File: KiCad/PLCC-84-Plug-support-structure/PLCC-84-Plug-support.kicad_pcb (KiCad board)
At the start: 2 copper layers, 29.6 x 29.6 mm, 4 parts, among them J1 Conn_01x01, J2 Conn_01x01, J3 Conn_01x01, J4 Conn_01x01

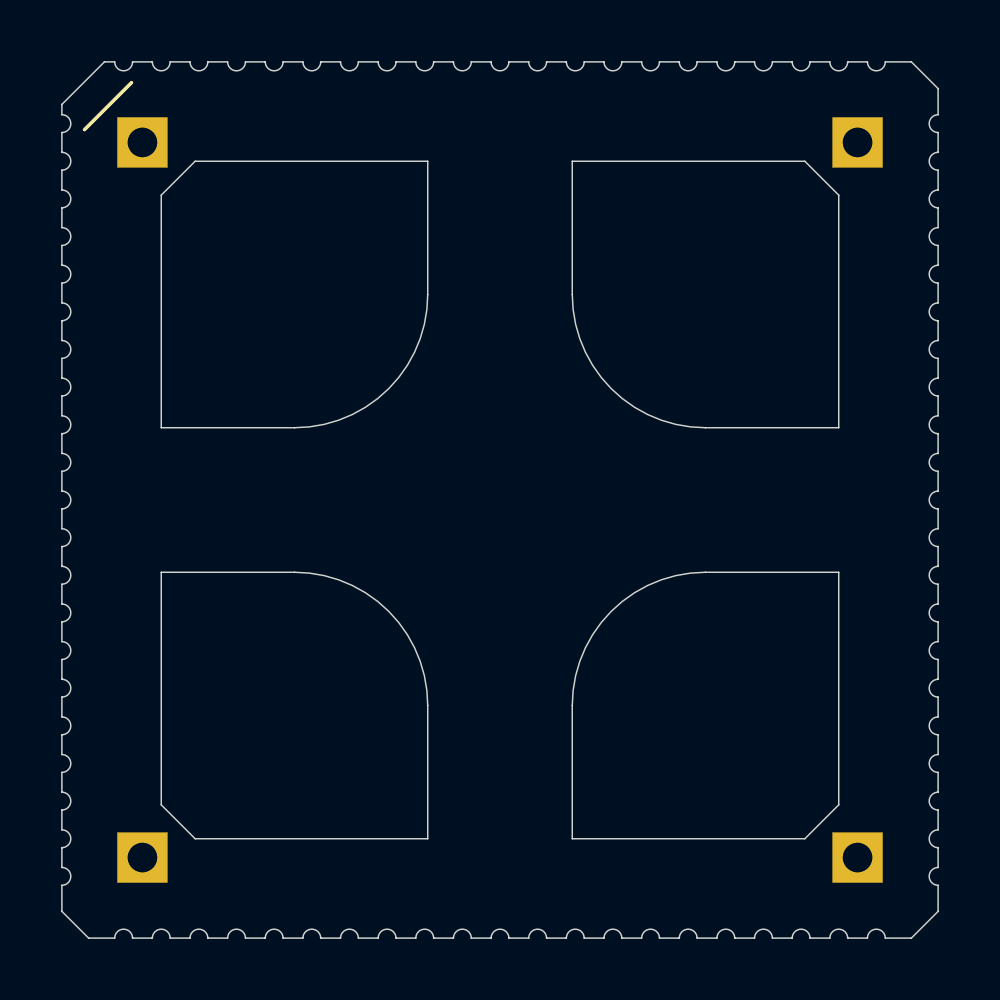
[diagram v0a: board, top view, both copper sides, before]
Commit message: made a new revision 1B with modified size
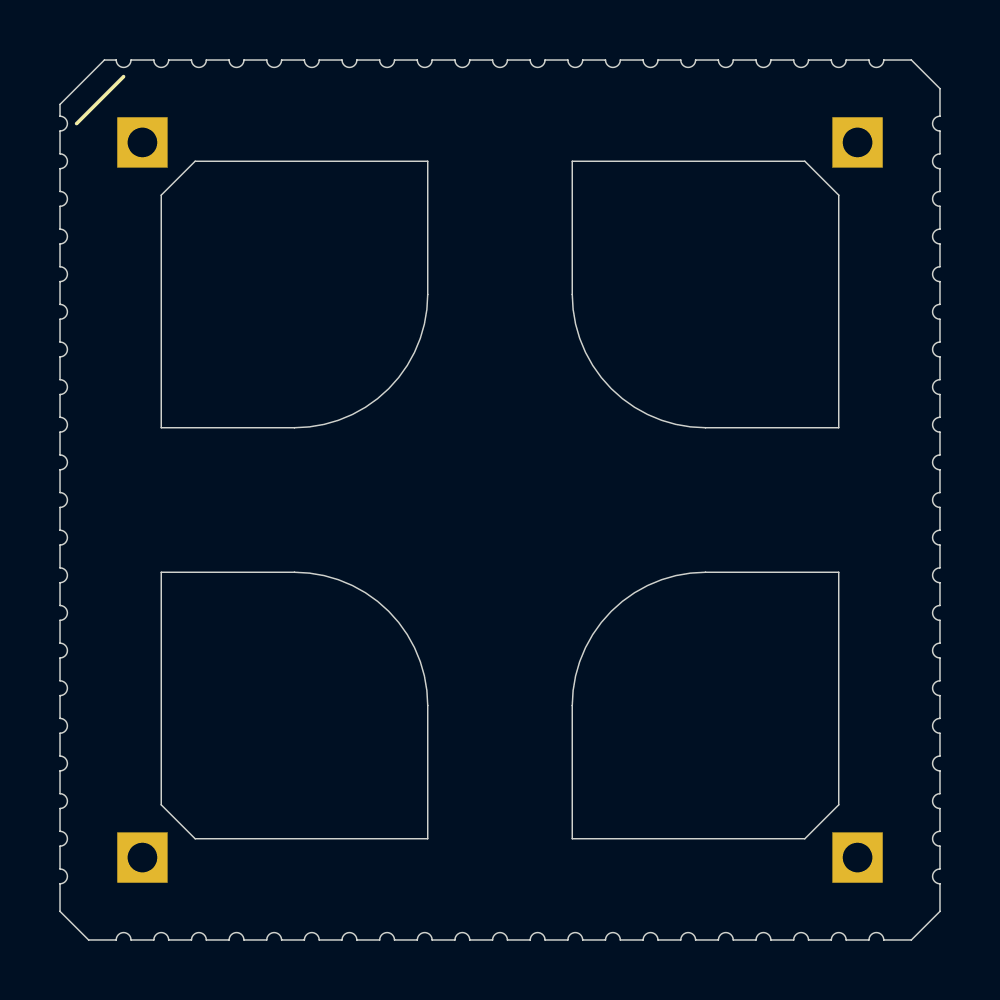
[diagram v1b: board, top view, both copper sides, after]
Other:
- board size 29.6 x 29.6 mm -> 29.7 x 29.7 mm
- board text added: "Rev. 1B"

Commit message: Re-design of dimensions and cut-outs to fit level-shifters on underside, Rev. 1C
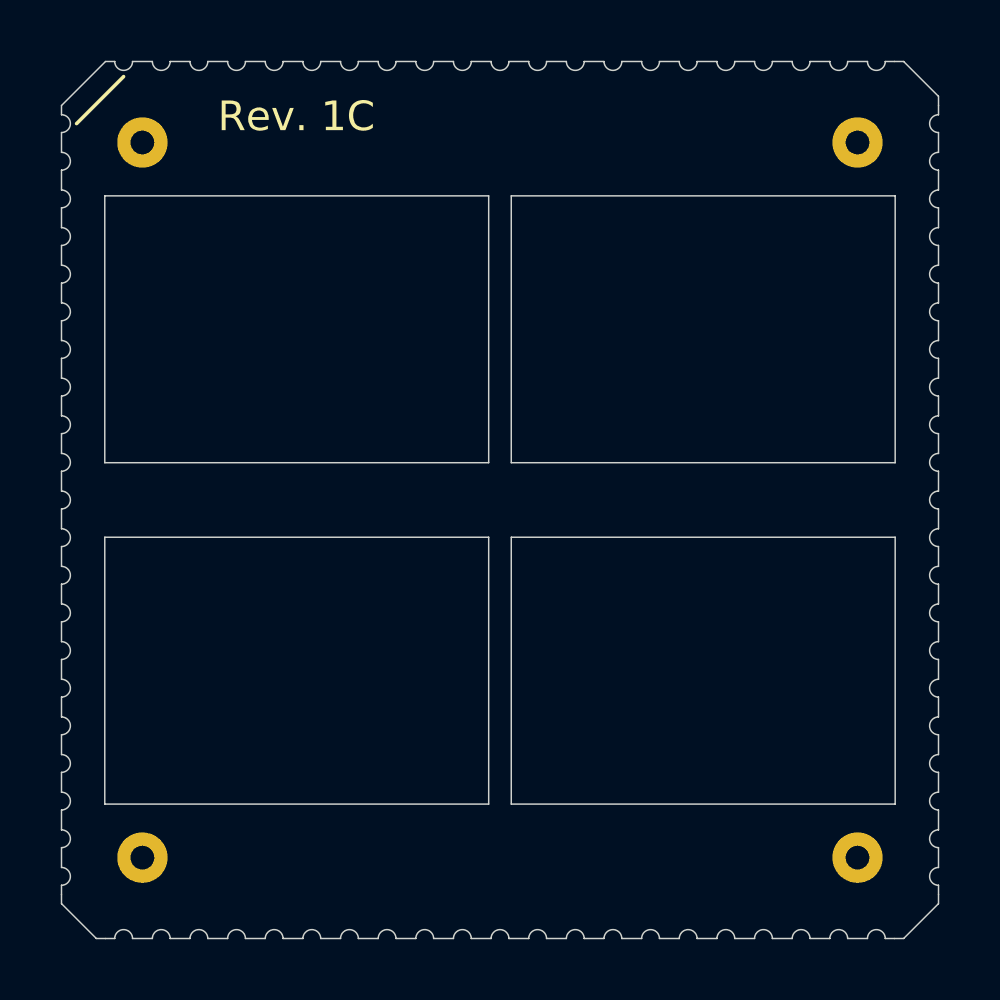
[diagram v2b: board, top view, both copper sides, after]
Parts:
- removed J1, J2, J3: Conn_01x01, Connector_PinHeader_2.54mm:PinHeader_1x01_P2.54mm_Vertical
- added J5: Conn_01x01, Connector_PinHeader_2.54mm:PinHeader_1x01_P2.54mm_Vertical, F.Cu at (104.8, 92.1)
- added J6: Conn_01x01, Connector_PinHeader_2.54mm:PinHeader_1x01_P2.54mm_Vertical, F.Cu at (80.6, 92.1)
- added J7: Conn_01x01, Connector_PinHeader_2.54mm:PinHeader_1x01_P2.54mm_Vertical, F.Cu at (80.6, 67.9)
- moved J4 24.1 mm to (104.8, 67.9), turned to 90 degrees
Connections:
- J4 pad 1: Net-(J4-Pad1) -> (no net)
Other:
- board size 29.7 x 29.7 mm -> 29.6 x 29.6 mm
- board text added: "Rev. 1C"
- board text removed: "Rev. 1B"

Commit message: small fix SolderMaskClearance setting
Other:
- rule pad_to_mask_clearance: 0.05 -> 0.0
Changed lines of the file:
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@@
     (pad_size 1.7 1.7)
     (pad_drill 0.8)
-    (pad_to_mask_clearance 0.05)
+    (pad_to_mask_clearance 0.0)
     (aux_axis_origin 0 0)
     (grid_origin 77.9137 65.2137)

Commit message: openframe version of Rev. 1C
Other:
- outline, holes or cut-outs redrawn
- rule pad_to_mask_clearance: 0.0 -> 0
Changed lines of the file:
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@@
   (general
     (thickness 1.6)
-    (drawings 201)
+    (drawings 189)
     (tracks 0)
     (zones 0)
@@
     (pad_size 1.7 1.7)
     (pad_drill 0.8)
-    (pad_to_mask_clearance 0.0)
+    (pad_to_mask_clearance 0)
     (aux_axis_origin 0 0)
     (grid_origin 77.9137 65.2137)
@@
       (effects (font (size 1 1) (thickness 0.15)))
     )
+    (fp_line (start -0.635 -1.27) (end 1.27 -1.27) (layer F.Fab) (width 0.1))
+    (fp_line (start 1.27 -1.27) (end 1.27 1.27) (layer F.Fab) (width 0.1))
+    (fp_line (start 1.27 1.27) (end -1.27 1.27) (layer F.Fab) (width 0.1))
+    (fp_line (start -1.27 1.27) (end -1.27 -0.635) (layer F.Fab) (width 0.1))
+    (fp_line (start -1.27 -0.635) (end -0.635 -1.27) (layer F.Fab) (width 0.1))
+    (fp_line (start -1.8 -1.8) (end -1.8 1.8) (layer F.CrtYd) (width 0.05))
+    (fp_line (start -1.8 1.8) (end 1.8 1.8) (layer F.CrtYd) (width 0.05))
+    (fp_line (start 1.8 1.8) (end 1.8 -1.8) (layer F.CrtYd) (width 0.05))
+    (fp_line (start 1.8 -1.8) (end -1.8 -1.8) (layer F.CrtYd) (width 0.05))
+    (fp_text user %R (at 0 0) (layer F.Fab) hide
+      (effects (font (size 1 1) (thickness 0.15)))
+    )
+    (pad 1 thru_hole oval (at 0 0 90) (size 1.7 1.7) (drill 0.8) (layers *.Cu *.Mask))
+  )
+  (module Connector_PinHeader_2.54mm:PinHeader_1x01_P2.54mm_Vertical (layer F.Cu)
+    (at 104.7738 92.0772)
+    (descr "Through hole straight pin header, 1x01, 2.54mm pitch, single row")
+    (tags "Through hole pin header THT 1x01 2.54mm single row")
+    (fp_text reference J5 (at 0 -2.33) (layer F.SilkS) hide
+      (effects (font (size 1 1) (thickness 0.15)))
+    )
+    (fp_text value Conn_01x01 (at 0 2.33) (layer F.Fab) hide
+      (effects (font (size 1 1) (thickness 0.15)))
+    )
+    (fp_line (start -0.635 -1.27) (end 1.27 -1.27) (layer F.Fab) (width 0.1))
+    (fp_line (start 1.27 -1.27) (end 1.27 1.27) (layer F.Fab) (width 0.1))
+    (fp_line (start 1.27 1.27) (end -1.27 1.27) (layer F.Fab) (width 0.1))
+    (fp_line (start -1.27 1.27) (end -1.27 -0.635) (layer F.Fab) (width 0.1))
+    (fp_line (start -1.27 -0.635) (end -0.635 -1.27) (layer F.Fab) (width 0.1))
+    (fp_line (start -1.8 -1.8) (end -1.8 1.8) (layer F.CrtYd) (width 0.05))
+    (fp_line (start -1.8 1.8) (end 1.8 1.8) (layer F.CrtYd) (width 0.05))
+    (fp_line (start 1.8 1.8) (end 1.8 -1.8) (layer F.CrtYd) (width 0.05))
+    (fp_line (start 1.8 -1.8) (end -1.8 -1.8) (layer F.CrtYd) (width 0.05))
+    (fp_text user %R (at 0 0 90) (layer F.Fab) hide
+      (effects (font (size 1 1) (thickness 0.15)))
+    )
+    (pad 1 thru_hole oval (at 0 0) (size 1.7 1.7) (drill 0.8) (layers *.Cu *.Mask))
+  )
+  (module Connector_PinHeader_2.54mm:PinHeader_1x01_P2.54mm_Vertical (layer F.Cu)
+    (at 80.6438 92.0772 270)
+    (descr "Through hole straight pin header, 1x01, 2.54mm pitch, single row")
+    (tags "Through hole pin header THT 1x01 2.54mm single row")
+    (fp_text reference J6 (at 0 -2.33 90) (layer F.SilkS) hide
+      (effects (font (size 1 1) (thickness 0.15)))
+    )
+    (fp_text value Conn_01x01 (at 0 2.33 90) (layer F.Fab) hide
+      (effects (font (size 1 1) (thickness 0.15)))
+    )
     (fp_line (start 1.8 -1.8) (end -1.8 -1.8) (layer F.CrtYd) (width 0.05))
     (fp_line (start 1.8 1.8) (end 1.8 -1.8) (layer F.CrtYd) (width 0.05))
@@
       (effects (font (size 1 1) (thickness 0.15)))
     )
-    (pad 1 thru_hole oval (at 0 0 90) (size 1.7 1.7) (drill 0.8) (layers *.Cu *.Mask))
+    (pad 1 thru_hole circle (at 0 0 270) (size 1.7 1.7) (drill 0.8) (layers *.Cu *.Mask))
   )
   (module Connector_PinHeader_2.54mm:PinHeader_1x01_P2.54mm_Vertical (layer F.Cu)
-    (at 104.7738 92.0772)
+    (at 80.6438 67.9472 180)
     (descr "Through hole straight pin header, 1x01, 2.54mm pitch, single row")
     (tags "Through hole pin header THT 1x01 2.54mm single row")
-    (fp_text reference J5 (at 0 -2.33) (layer F.SilkS) hide
+    (fp_text reference J7 (at 0 -2.33) (layer F.SilkS) hide
       (effects (font (size 1 1) (thickness 0.15)))
     )
     (fp_text value Conn_01x01 (at 0 2.33) (layer F.Fab) hide
-      (effects (font (size 1 1) (thickness 0.15)))
-    )
-    (fp_line (start 1.8 -1.8) (end -1.8 -1.8) (layer F.CrtYd) (width 0.05))
-    (fp_line (start 1.8 1.8) (end 1.8 -1.8) (layer F.CrtYd) (width 0.05))
-    (fp_line (start -1.8 1.8) (end 1.8 1.8) (layer F.CrtYd) (width 0.05))
-    (fp_line (start -1.8 -1.8) (end -1.8 1.8) (layer F.CrtYd) (width 0.05))
-    (fp_line (start -1.27 -0.635) (end -0.635 -1.27) (layer F.Fab) (width 0.1))
-    (fp_line (start -1.27 1.27) (end -1.27 -0.635) (layer F.Fab) (width 0.1))
-    (fp_line (start 1.27 1.27) (end -1.27 1.27) (layer F.Fab) (width 0.1))
-    (fp_line (start 1.27 -1.27) (end 1.27 1.27) (layer F.Fab) (width 0.1))
-    (fp_line (start -0.635 -1.27) (end 1.27 -1.27) (layer F.Fab) (width 0.1))
-    (fp_text user %R (at 0 0 90) (layer F.Fab) hide
-      (effects (font (size 1 1) (thickness 0.15)))
-    )
-    (pad 1 thru_hole oval (at 0 0) (size 1.7 1.7) (drill 0.8) (layers *.Cu *.Mask))
-  )
-  (module Connector_PinHeader_2.54mm:PinHeader_1x01_P2.54mm_Vertical (layer F.Cu)
-    (at 80.6438 92.0772 270)
-    (descr "Through hole straight pin header, 1x01, 2.54mm pitch, single row")
-    (tags "Through hole pin header THT 1x01 2.54mm single row")
-    (fp_text reference J6 (at 0 -2.33 90) (layer F.SilkS) hide
-      (effects (font (size 1 1) (thickness 0.15)))
-    )
-    (fp_text value Conn_01x01 (at 0 2.33 90) (layer F.Fab) hide
       (effects (font (size 1 1) (thickness 0.15)))
     )
@@
     (fp_line (start 1.8 1.8) (end 1.8 -1.8) (layer F.CrtYd) (width 0.05))
     (fp_line (start 1.8 -1.8) (end -1.8 -1.8) (layer F.CrtYd) (width 0.05))
-    (fp_text user %R (at 0 0) (layer F.Fab) hide
-      (effects (font (size 1 1) (thickness 0.15)))
-    )
-    (pad 1 thru_hole circle (at 0 0 270) (size 1.7 1.7) (drill 0.8) (layers *.Cu *.Mask))
-  )
-  (module Connector_PinHeader_2.54mm:PinHeader_1x01_P2.54mm_Vertical (layer F.Cu)
-    (at 80.6438 67.9472 180)
-    (descr "Through hole straight pin header, 1x01, 2.54mm pitch, single row")
-    (tags "Through hole pin header THT 1x01 2.54mm single row")
-    (fp_text reference J7 (at 0 -2.33) (layer F.SilkS) hide
-      (effects (font (size 1 1) (thickness 0.15)))
-    )
-    (fp_text value Conn_01x01 (at 0 2.33) (layer F.Fab) hide
-      (effects (font (size 1 1) (thickness 0.15)))
-    )
-    (fp_line (start 1.8 -1.8) (end -1.8 -1.8) (layer F.CrtYd) (width 0.05))
-    (fp_line (start 1.8 1.8) (end 1.8 -1.8) (layer F.CrtYd) (width 0.05))
-    (fp_line (start -1.8 1.8) (end 1.8 1.8) (layer F.CrtYd) (width 0.05))
-    (fp_line (start -1.8 -1.8) (end -1.8 1.8) (layer F.CrtYd) (width 0.05))
-    (fp_line (start -1.27 -0.635) (end -0.635 -1.27) (layer F.Fab) (width 0.1))
-    (fp_line (start -1.27 1.27) (end -1.27 -0.635) (layer F.Fab) (width 0.1))
-    (fp_line (start 1.27 1.27) (end -1.27 1.27) (layer F.Fab) (width 0.1))
-    (fp_line (start 1.27 -1.27) (end 1.27 1.27) (layer F.Fab) (width 0.1))
-    (fp_line (start -0.635 -1.27) (end 1.27 -1.27) (layer F.Fab) (width 0.1))
     (fp_text user %R (at 0 0 90) (layer F.Fab) hide
       (effects (font (size 1 1) (thickness 0.15)))
@@
     (pad 1 thru_hole oval (at 0 0 180) (size 1.7 1.7) (drill 0.8) (layers *.Cu *.Mask))
   )
-  (gr_line (start 92.3282 90.2708) (end 92.3282 81.2665) (layer Edge.Cuts) (width 0.05))
-  (gr_line (start 79.3742 90.2708) (end 92.3282 90.2708) (layer Edge.Cuts) (width 0.05))
-  (gr_line (start 106.0442 81.2665) (end 93.0902 81.2665) (layer Edge.Cuts) (width 0.05))
-  (gr_line (start 93.0902 90.2708) (end 93.0902 81.2665) (layer Edge.Cuts) (width 0.05))
-  (gr_line (start 106.0442 90.2708) (end 106.0442 81.2665) (layer Edge.Cuts) (width 0.05))
-  (gr_line (start 106.0442 78.7519) (end 93.0902 78.7519) (layer Edge.Cuts) (width 0.05))
-  (gr_line (start 79.3742 90.2708) (end 79.3742 81.2665) (layer Edge.Cuts) (width 0.05))
-  (gr_line (start 92.3282 81.2665) (end 79.3742 81.2665) (layer Edge.Cuts) (width 0.05))
-  (gr_line (start 92.3282 78.7519) (end 79.3742 78.7519) (layer Edge.Cuts) (width 0.05))
-  (gr_line (start 93.0902 78.7519) (end 93.0902 69.7476) (layer Edge.Cuts) (width 0.05))
-  (gr_line (start 93.0902 90.2708) (end 106.0442 90.2708) (layer Edge.Cuts) (width 0.05))
-  (gr_line (start 93.0902 69.7476) (end 106.0442 69.7476) (layer Edge.Cuts) (width 0.05))
-  (gr_line (start 79.3742 69.7476) (end 92.3282 69.7476) (layer Edge.Cuts) (width 0.05))
-  (gr_line (start 106.0442 78.7519) (end 106.0442 69.7476) (layer Edge.Cuts) (width 0.05))
-  (gr_line (start 79.3742 78.7519) (end 79.3742 69.7476) (layer Edge.Cuts) (width 0.05))
+  (gr_line (start 79.3742 90.2708) (end 106.0442 90.2708) (layer Edge.Cuts) (width 0.05))
+  (gr_line (start 79.3742 69.7476) (end 106.0442 69.7476) (layer Edge.Cuts) (width 0.05))
+  (gr_line (start 106.0442 90.2708) (end 106.0442 69.7476) (layer Edge.Cuts) (width 0.05))
+  (gr_line (start 79.3742 90.2708) (end 79.3742 69.7476) (layer Edge.Cuts) (width 0.05))
   (gr_line (start 79.3996 94.8063) (end 79.0892 94.8063) (layer Edge.Cuts) (width 0.05))
   (gr_line (start 77.9137 93.6308) (end 77.9137 93.3204) (layer Edge.Cuts) (width 0.05))
@@
   )
   (gr_line (start 78.4225 67.31) (end 80.01 65.7225) (layer F.SilkS) (width 0.12))
-  (gr_line (start 92.3282 78.7519) (end 92.3282 69.7476) (layer Edge.Cuts) (width 0.05))
 )
